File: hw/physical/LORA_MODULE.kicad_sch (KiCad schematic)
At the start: 6 parts, among them J3 Conn_Coaxial, U2 RFM69HCW

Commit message: - Consolidate POWER and BATTERY pages - Updated 1.8V SYS REG to low Iq option - Replaced LoRA module with SemTech transceiver - Adding latest nRF datasheet
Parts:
- removed C10, C16, C17: C_Small, symbol Device:C_Small
- removed J3: Conn_Coaxial, symbol Connector:Conn_Coaxial
- removed L4: L, symbol Device:L
- removed U2: RFM69HCW, RF_Module:HOPERF_RFM9XW_SMD, symbol RF_Module:RFM69HCW
- added C301, C302, C303, C304, C305, C306, C310, C311: C_Small, symbol Device:C_Small
- added C307: 10p, symbol Device:C_Small
- added C308: 100N, symbol Device:C_Small
- added C309: 1U, symbol Device:C_Small
- added J301: Conn_Coaxial, symbol Connector:Conn_Coaxial
- added L301: L, symbol Device:L
- added R301, R303: 100K, symbol Device:R
- added R302: 22R, symbol Device:R
- added U301: SX1276, Package_DFN_QFN:QFN-28-1EP_6x6mm_P0.65mm_EP4.8x4.8mm, symbol RF:SX1276
- added X302: SG-5032CAN, Oscillator:Oscillator_SMD_SeikoEpson_SG8002LB-4Pin_5.0x3.2mm, symbol Oscillator:SG-5032CAN
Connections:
- net GND: now also C301.2, C302.2, C303.2, C304.2, C305.2, C306.2, C307.2, C308.2, C309.2, C310.2, C311.2, J301.2 (Ext), R301.1, R303.1, U301.15 (GND), U301.23 (GND), U301.26 (GND), U301.29 (GND), X302.2 (GND)
- net LORA_RST: now also R301.2, U301.7 (~{RESET})
- net SPI_LORA_CLK: now also U301.16 (SCK)
- net SPI_LORA_CS_L: now also U301.19 (NSS)
- net SPI_LORA_DO_NRF_DI: now also U301.17 (MISO)
- net SPI_NRF_DO_LORA_DI: now also U301.18 (MOSI)
- new net: C301.1, C302.1, C303.1, C304.1, U301.24 (VBAT_RF)
- new net: C306.1, U301.3 (VBAT_ANA)
- new net: C307.1, R302.1, U301.5 (XTA)
- new net: C310.1, L301.1
- new net: C311.1, J301.1 (In), L301.2
- new net: R302.2, X302.3 (OUT)
- new net LORA_EXT_CLK_OUT: U301.13 (DIO5)
- new net LORA_XTN_CLK_EN: R303.2, X302.1 (~{ST})
- new net PP1800_ALW: C305.1, C308.1, C309.1, U301.14 (VBAT_DIG), X302.4 (VCC)
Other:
- note added: "NEED RFFE POP-OPTIONS FOR SUPPORTED BANDS"
- note added: "SG2016CAN32.000000MHzTDBA"
- note removed: "REPLACE WITH SEMTECH PART"

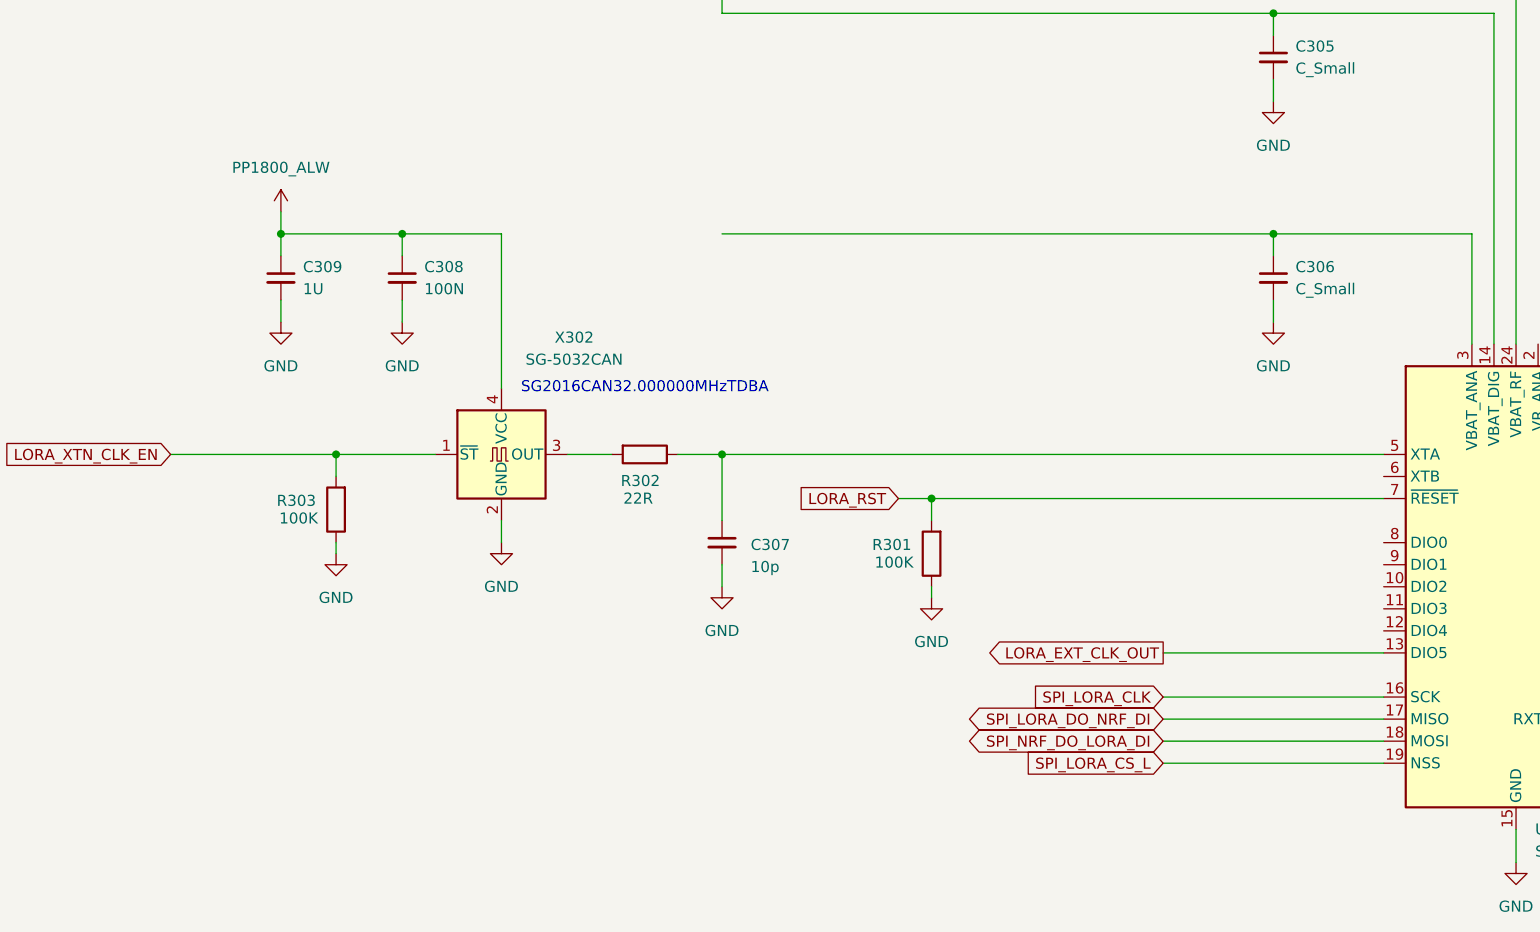
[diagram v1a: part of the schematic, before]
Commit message: Adding nRF54L10 schematic library component. Redrew MCU page with nRF54L10 and rearranged or changed net labels and global labels.
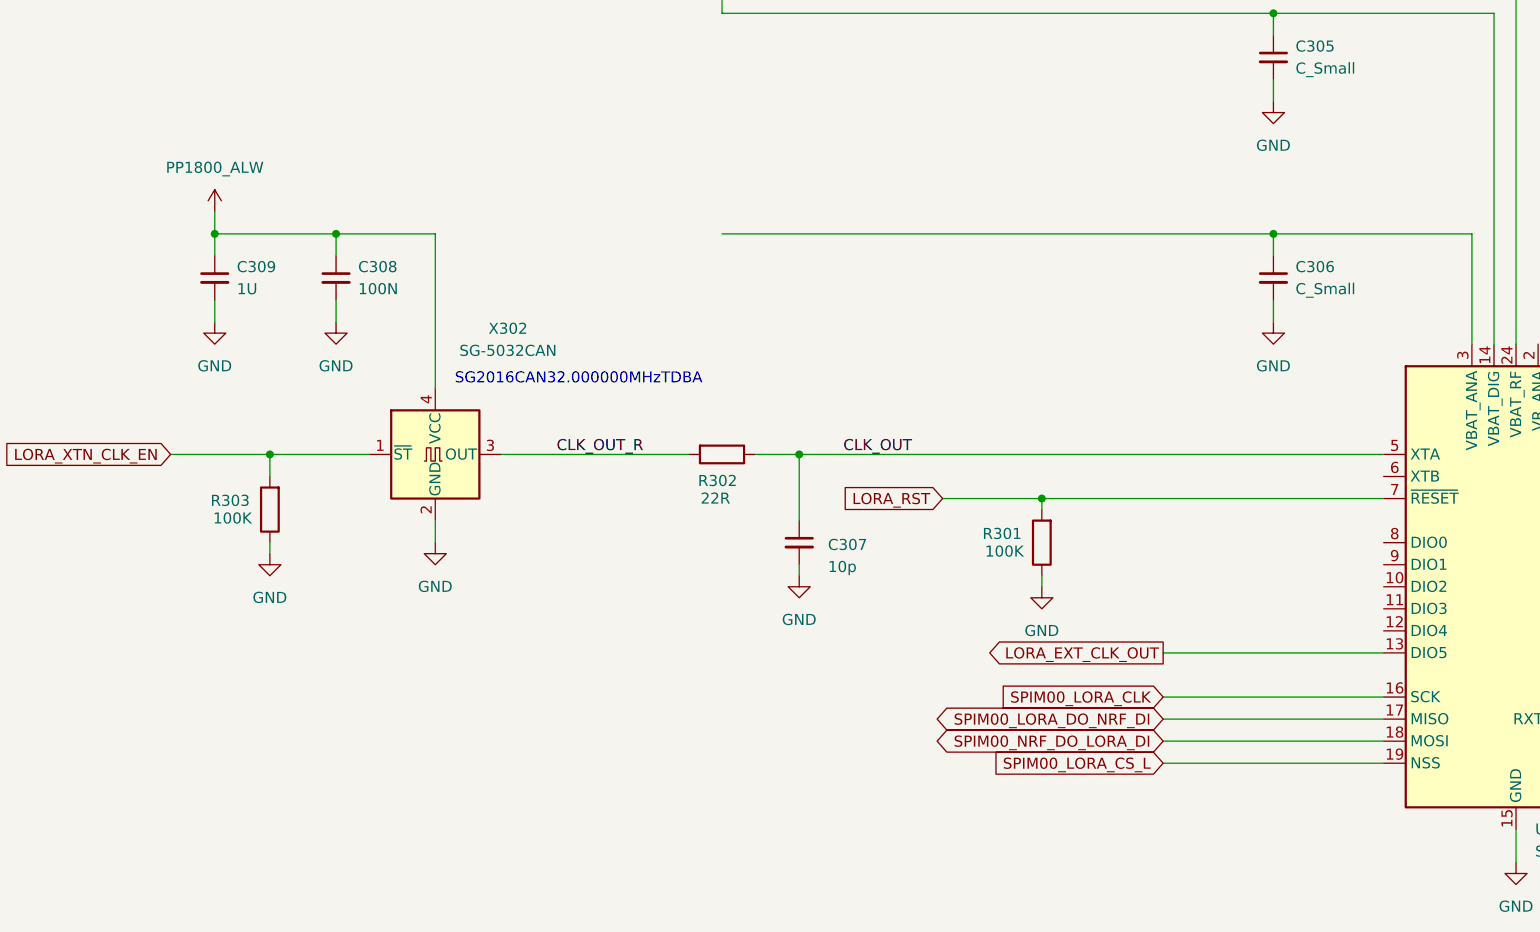
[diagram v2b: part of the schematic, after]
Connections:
- net CLK_OUT: now reaches C307.1, R302.1, U301.5 (XTA)
- net CLK_OUT_R: now reaches R302.2, X302.3 (OUT)
- net SPI_LORA_CLK renamed SPIM00_LORA_CLK
- net SPI_LORA_CS_L renamed SPIM00_LORA_CS_L
- net SPI_LORA_DO_NRF_DI renamed SPIM00_LORA_DO_NRF_DI
- net SPI_NRF_DO_LORA_DI renamed SPIM00_NRF_DO_LORA_DI
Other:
- moved on the sheet: C307, C308, C309, R301, R302, R303, X302

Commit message: Various Schematic Modifications and Additions. * Removed Bypass page and moved bypass caps to MCU page. * Moved MCU VSS_PA pin to logical location as per Nordic guidelines. * Added Display Circuit, level shifters, charge pump, connector, etc. * Added 3.3V display VREG with Enable GPIO. * Added BLE RF components as per Nordic guidelines. * Added DCC circuit as per Nordic guidelines. * Rearranged GPIO's and interfaces. * Fixed various schematic errors.
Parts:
- renumbered C304 to C301, C303 to C302, C302 to C303, C301 to C304, C309 to C306, C308 to C307, C306 to C308, C307 to C309, R302 to R301, R303 to R302, R301 to R303, X302 to X301
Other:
- note added: "LoRA Radio"
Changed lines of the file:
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@@
+		)
+	)
+	(text "LoRA Radio"
+		(exclude_from_sim no)
+		(at 41.91 23.622 0)
+		(effects
+			(font
+				(size 5 5)
+			)
 		)
 	)
@@
 		(dnp no)
 		(fields_autoplaced yes)
-		(property "Reference" "C301"
+		(property "Reference" "C304"
 			(at 167.64 46.9962 0)
 			(effects
@@
 			(project "lora_radio_lp"
 				(path "/fff85bc4-e8ec-4b5d-b2e2-83ecb397a864/58c3d426-d3ca-4263-a439-0e9101a026f3"
-					(reference "C301")
+					(reference "C304")
 					(unit 1)
 				)
@@
 		(dnp no)
 		(fields_autoplaced yes)
-		(property "Reference" "C309"
+		(property "Reference" "C306"
 			(at 45.72 97.7962 0)
 			(effects
@@
 			(project "lora_radio_lp"
 				(path "/fff85bc4-e8ec-4b5d-b2e2-83ecb397a864/58c3d426-d3ca-4263-a439-0e9101a026f3"
-					(reference "C309")
+					(reference "C306")
 					(unit 1)
 				)
@@
 		(on_board yes)
 		(dnp no)
-		(property "Reference" "R301"
+		(property "Reference" "R303"
 			(at 133.858 128.524 0)
 			(effects
@@
 			(project "lora_radio_lp"
 				(path "/fff85bc4-e8ec-4b5d-b2e2-83ecb397a864/58c3d426-d3ca-4263-a439-0e9101a026f3"
-					(reference "R301")
+					(reference "R303")
 					(unit 1)
 				)
@@
 		(dnp no)
 		(fields_autoplaced yes)
-		(property "Reference" "#PWR0310"
+		(property "Reference" "#PWR0311"
 			(at 68.58 135.89 0)
 			(effects
@@
 			(project "lora_radio_lp"
 				(path "/fff85bc4-e8ec-4b5d-b2e2-83ecb397a864/58c3d426-d3ca-4263-a439-0e9101a026f3"
-					(reference "#PWR0310")
+					(reference "#PWR0311")
 					(unit 1)
 				)
@@
 		(dnp no)
 		(fields_autoplaced yes)
-		(property "Reference" "#PWR0302"
+		(property "Reference" "#PWR0304"
 			(at 165.1 59.69 0)
 			(effects
@@
 			(project "lora_radio_lp"
 				(path "/fff85bc4-e8ec-4b5d-b2e2-83ecb397a864/58c3d426-d3ca-4263-a439-0e9101a026f3"
-					(reference "#PWR0302")
+					(reference "#PWR0304")
 					(unit 1)
 				)
@@
 		(dnp no)
 		(fields_autoplaced yes)
-		(property "Reference" "#PWR0301"
+		(property "Reference" "#PWR0318"
 			(at 193.04 172.72 0)
 			(effects
@@
 			(project "lora_radio_lp"
 				(path "/fff85bc4-e8ec-4b5d-b2e2-83ecb397a864/58c3d426-d3ca-4263-a439-0e9101a026f3"
-					(reference "#PWR0301")
+					(reference "#PWR0318")
 					(unit 1)
 				)
@@
 		(dnp no)
 		(fields_autoplaced yes)
-		(property "Reference" "#PWR0305"
+		(property "Reference" "#PWR0301"
 			(at 114.3 59.69 0)
 			(effects
@@
 			(project "lora_radio_lp"
 				(path "/fff85bc4-e8ec-4b5d-b2e2-83ecb397a864/58c3d426-d3ca-4263-a439-0e9101a026f3"
-					(reference "#PWR0305")
+					(reference "#PWR0301")
 					(unit 1)
 				)
@@
 		(on_board yes)
 		(dnp no)
-		(property "Reference" "R302"
+		(property "Reference" "R301"
 			(at 101.092 122.428 90)
 			(effects
@@
 			(project "lora_radio_lp"
 				(path "/fff85bc4-e8ec-4b5d-b2e2-83ecb397a864/58c3d426-d3ca-4263-a439-0e9101a026f3"
-					(reference "R302")
+					(reference "R301")
 					(unit 1)
 				)
@@
 		(dnp no)
 		(fields_autoplaced yes)
-		(property "Reference" "C304"
+		(property "Reference" "C301"
 			(at 116.84 46.9962 0)
 			(effects
@@
 			(project "lora_radio_lp"
 				(path "/fff85bc4-e8ec-4b5d-b2e2-83ecb397a864/58c3d426-d3ca-4263-a439-0e9101a026f3"
-					(reference "C304")
+					(reference "C301")
 					(unit 1)
 				)
@@
 		(on_board yes)
 		(dnp no)
-		(property "Reference" "C307"
+		(property "Reference" "C309"
 			(at 113.792 129.794 0)
 			(effects
@@
 			(project "lora_radio_lp"
 				(path "/fff85bc4-e8ec-4b5d-b2e2-83ecb397a864/58c3d426-d3ca-4263-a439-0e9101a026f3"
-					(reference "C307")
+					(reference "C309")
 					(unit 1)
 				)
@@
 		(dnp no)
 		(fields_autoplaced yes)
-		(property "Reference" "#PWR0309"
+		(property "Reference" "#PWR0314"
 			(at 138.43 140.97 0)
 			(effects
@@
 			(project "lora_radio_lp"
 				(path "/fff85bc4-e8ec-4b5d-b2e2-83ecb397a864/58c3d426-d3ca-4263-a439-0e9101a026f3"
-					(reference "#PWR0309")
+					(reference "#PWR0314")
 					(unit 1)
 				)
@@
 		(dnp no)
 		(fields_autoplaced yes)
-		(property "Reference" "#PWR0315"
+		(property "Reference" "#PWR0308"
 			(at 43.18 110.49 0)
 			(effects
@@
 			(project "lora_radio_lp"
 				(path "/fff85bc4-e8ec-4b5d-b2e2-83ecb397a864/58c3d426-d3ca-4263-a439-0e9101a026f3"
-					(reference "#PWR0315")
+					(reference "#PWR0308")
 					(unit 1)
 				)
@@
 		(on_board yes)
 		(dnp no)
-		(property "Reference" "X302"
+		(property "Reference" "X301"
 			(at 76.962 104.902 0)
 			(effects
@@
 			(project ""
 				(path "/fff85bc4-e8ec-4b5d-b2e2-83ecb397a864/58c3d426-d3ca-4263-a439-0e9101a026f3"
-					(reference "X302")
+					(reference "X301")
 					(unit 1)
 				)
@@
 		(dnp no)
 		(fields_autoplaced yes)
-		(property "Reference" "#PWR0304"
+		(property "Reference" "#PWR0302"
 			(at 132.08 59.69 0)
 			(effects
@@
 			(project "lora_radio_lp"
 				(path "/fff85bc4-e8ec-4b5d-b2e2-83ecb397a864/58c3d426-d3ca-4263-a439-0e9101a026f3"
-					(reference "#PWR0304")
+					(reference "#PWR0302")
 					(unit 1)
 				)
@@
 		(dnp no)
 		(fields_autoplaced yes)
-		(property "Reference" "#PWR0318"
+		(property "Reference" "#PWR0315"
 			(at 383.54 140.97 0)
 			(effects
@@
 			(project "lora_radio_lp"
 				(path "/fff85bc4-e8ec-4b5d-b2e2-83ecb397a864/58c3d426-d3ca-4263-a439-0e9101a026f3"
-					(reference "#PWR0318")
+					(reference "#PWR0315")
 					(unit 1)
 				)
@@
 		(dnp no)
 		(fields_autoplaced yes)
-		(property "Reference" "C303"
+		(property "Reference" "C302"
 			(at 134.62 46.9962 0)
 			(effects
@@
 			(project "lora_radio_lp"
 				(path "/fff85bc4-e8ec-4b5d-b2e2-83ecb397a864/58c3d426-d3ca-4263-a439-0e9101a026f3"
-					(reference "C303")
+					(reference "C302")
 					(unit 1)
 				)
@@
 		(on_board yes)
 		(dnp no)
-		(property "Reference" "R303"
+		(property "Reference" "R302"
 			(at 44.958 124.714 0)
 			(effects
@@
 			(project "lora_radio_lp"
 				(path "/fff85bc4-e8ec-4b5d-b2e2-83ecb397a864/58c3d426-d3ca-4263-a439-0e9101a026f3"
-					(reference "R303")
+					(reference "R302")
 					(unit 1)
 				)
@@
 		(dnp no)
 		(fields_autoplaced yes)
-		(property "Reference" "#PWR0307"
+		(property "Reference" "#PWR0310"
 			(at 165.1 110.49 0)
 			(effects
@@
 			(project "lora_radio_lp"
 				(path "/fff85bc4-e8ec-4b5d-b2e2-83ecb397a864/58c3d426-d3ca-4263-a439-0e9101a026f3"
-					(reference "#PWR0307")
+					(reference "#PWR0310")
 					(unit 1)
 				)
@@
 		(dnp no)
 		(fields_autoplaced yes)
-		(property "Reference" "C302"
+		(property "Reference" "C303"
 			(at 151.13 46.9962 0)
 			(effects
@@
 			(project "lora_radio_lp"
 				(path "/fff85bc4-e8ec-4b5d-b2e2-83ecb397a864/58c3d426-d3ca-4263-a439-0e9101a026f3"
-					(reference "C302")
+					(reference "C303")
 					(unit 1)
 				)
@@
 		(dnp no)
 		(fields_autoplaced yes)
-		(property "Reference" "#PWR0313"
+		(property "Reference" "#PWR0307"
 			(at 43.18 95.25 0)
 			(effects
@@
 			(project "lora_radio_lp"
 				(path "/fff85bc4-e8ec-4b5d-b2e2-83ecb397a864/58c3d426-d3ca-4263-a439-0e9101a026f3"
-					(reference "#PWR0313")
+					(reference "#PWR0307")
 					(unit 1)
 				)
@@
 		(dnp no)
 		(fields_autoplaced yes)
-		(property "Reference" "#PWR0308"
+		(property "Reference" "#PWR0305"
 			(at 101.6 69.85 0)
 			(effects
@@
 			(project "lora_radio_lp"
 				(path "/fff85bc4-e8ec-4b5d-b2e2-83ecb397a864/58c3d426-d3ca-4263-a439-0e9101a026f3"
-					(reference "#PWR0308")
+					(reference "#PWR0305")
 					(unit 1)
 				)
@@
 		(dnp no)
 		(fields_autoplaced yes)
-		(property "Reference" "#PWR0314"
+		(property "Reference" "#PWR0309"
 			(at 57.15 110.49 0)
 			(effects
@@
 			(project "lora_radio_lp"
 				(path "/fff85bc4-e8ec-4b5d-b2e2-83ecb397a864/58c3d426-d3ca-4263-a439-0e9101a026f3"
-					(reference "#PWR0314")
+					(reference "#PWR0309")
 					(unit 1)
 				)
@@
 		(dnp no)
 		(fields_autoplaced yes)
-		(property "Reference" "#PWR0311"
+		(property "Reference" "#PWR0313"
 			(at 110.49 139.7 0)
 			(effects
@@
 			(project "lora_radio_lp"
 				(path "/fff85bc4-e8ec-4b5d-b2e2-83ecb397a864/58c3d426-d3ca-4263-a439-0e9101a026f3"
-					(reference "#PWR0311")
+					(reference "#PWR0313")
 					(unit 1)
 				)
@@
 		(dnp no)
 		(fields_autoplaced yes)
-		(property "Reference" "C308"
+		(property "Reference" "C307"
 			(at 59.69 97.7962 0)
 			(effects
@@
 			(project "lora_radio_lp"
 				(path "/fff85bc4-e8ec-4b5d-b2e2-83ecb397a864/58c3d426-d3ca-4263-a439-0e9101a026f3"
-					(reference "C308")
+					(reference "C307")
 					(unit 1)
 				)
@@
 		(dnp no)
 		(fields_autoplaced yes)
-		(property "Reference" "C306"
+		(property "Reference" "C308"
 			(at 167.64 97.7962 0)
 			(effects
@@
 			(project "lora_radio_lp"
 				(path "/fff85bc4-e8ec-4b5d-b2e2-83ecb397a864/58c3d426-d3ca-4263-a439-0e9101a026f3"
-					(reference "C306")
-					(unit 1)
-				)
+					(reference "C308")
+					(unit 1)
+				)
